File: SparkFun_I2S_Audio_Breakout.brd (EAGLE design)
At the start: 20.3 x 20.3 mm, 42 parts, among them IC1 MAX98375A

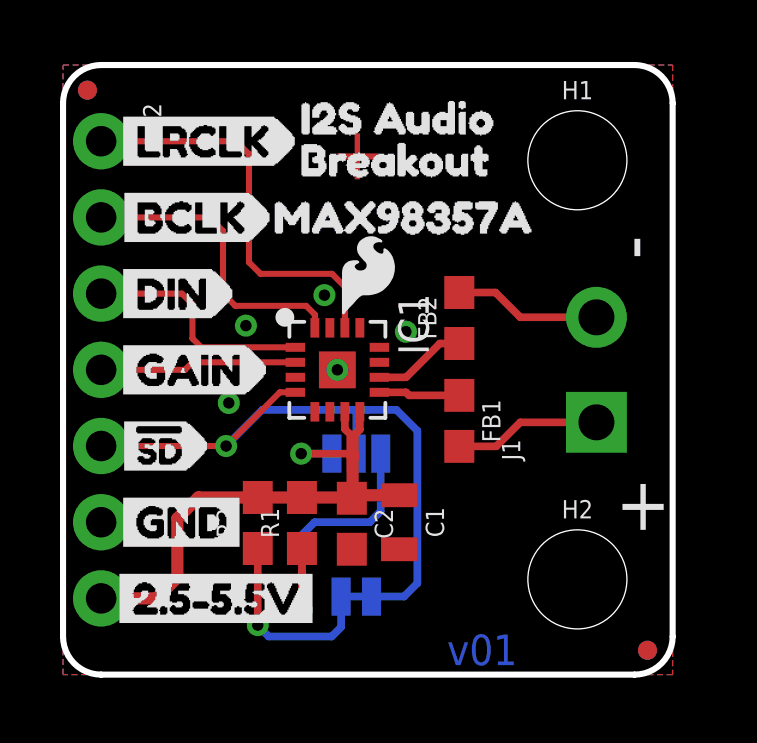
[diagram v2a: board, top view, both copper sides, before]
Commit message: v10
Removed + symbol on top copper
Removed ferrite beads
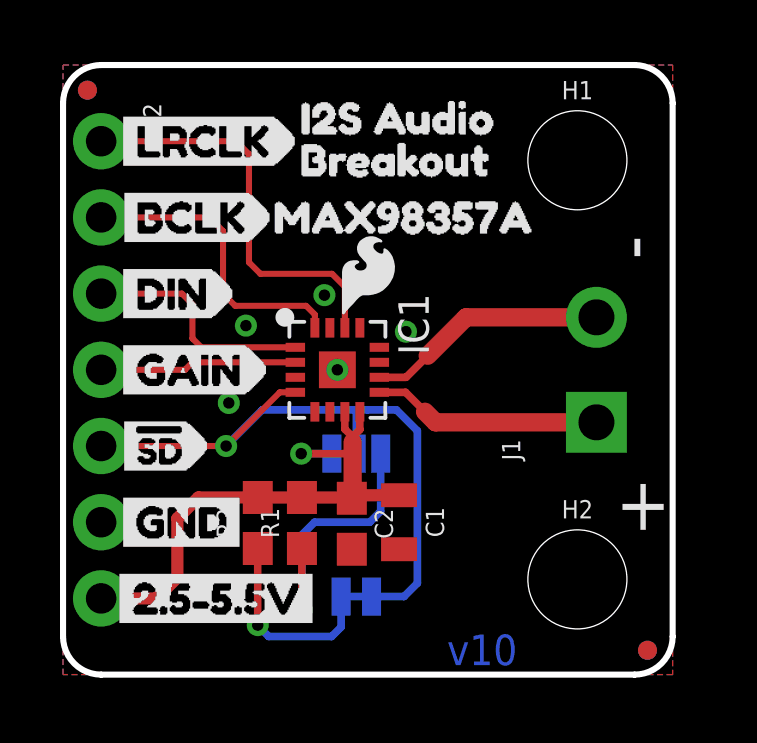
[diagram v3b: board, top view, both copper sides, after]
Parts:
- removed FB1, FB2: (no value), SparkFun-Coils:0603
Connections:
- removed net N$1: FB1.1, IC1.P$9
- removed net N$2: FB2.1, IC1.P$10
- removed net N$3: FB1.2, J1.1
- removed net N$4: FB2.2, J1.2
- new net OUT+: IC1.P$9, J1.1
- new net OUT-: IC1.P$10, J1.2
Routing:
- net OUT-: track 0.00 -> 8.06 mm
- net OUT+: track 0.00 -> 7.65 mm
- net N$4: track 4.92 -> 0.00 mm
- net N$3: track 4.90 -> 0.00 mm
- net N$2: track 3.13 -> 0.00 mm
- net N$1: track 2.85 -> 0.00 mm
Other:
- board text added: "v10"
- board text removed: "v01"
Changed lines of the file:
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@@
 <?xml version="1.0" encoding="utf-8"?>
 <!DOCTYPE eagle SYSTEM "eagle.dtd">
-<eagle version="9.0.1">
+<eagle version="9.1.1">
 <drawing>
 <settings>
@@
 <wire x1="9.865359375" y1="10.287" x2="9.865359375" y2="10.033" width="0.2032" layer="41"/>
 <wire x1="9.017" y1="9.44118125" x2="9.271" y2="9.44118125" width="0.2032" layer="41"/>
-<text x="13.97" y="0.3175" size="1.016" layer="16" font="vector" ratio="20" rot="SR0" align="bottom-center">v01</text>
+<text x="13.97" y="0.3175" size="1.016" layer="16" font="vector" ratio="20" rot="SR0" align="bottom-center">v10</text>
 <text x="12.7635" y="-18.288" size="2.1844" layer="51" font="vector" ratio="15" align="center-left">Alex Wende</text>
 <dimension x1="0" y1="1.27" x2="20.32" y2="1.27" x3="10.16" y3="-5.08" textsize="1.27" textratio="15" layer="47" unit="inch"/>
@@
 <text x="5.08" y="-6.35" size="1.27" layer="47" font="vector" ratio="15" align="center-left">Units: Inches</text>
 <dimension x1="1.27" y1="2.54" x2="1.27" y2="0" x3="-2.54" y3="1.27" textsize="1.27" textratio="15" layer="47" unit="inch" precision="3"/>
-<text x="8.89" y="16.51" size="1.778" layer="1" font="vector" ratio="16">+</text>
 <text x="18.415" y="4.826" size="1.778" layer="21" font="vector" ratio="15">+</text>
 <text x="19.812" y="13.843" size="1.778" layer="21" font="vector" ratio="15" rot="R90">-</text>
@@
 <param name="checkStop" value="0"/>
 <param name="checkValues" value="0"/>
+<param name="checkNames" value="1"/>
+<param name="checkWireStubs" value="1"/>
+<param name="checkPolygonWidth" value="0"/>
 <param name="useDiameter" value="13"/>
 <param name="maxErrors" value="50"/>
@@
 <attribute name="PROD_ID" value="CAP-00810" x="9.6266" y="5.0292" size="1.778" layer="27" rot="R270" display="off"/>
 </element>
-<element name="FB1" library="SparkFun-Coils" package="0603" value="" x="13.208" y="8.4582" rot="R270">
-<attribute name="PROD_ID" value="NDUC-13805" x="13.208" y="8.4582" size="1.778" layer="27" rot="R270" display="off"/>
-</element>
-<element name="FB2" library="SparkFun-Coils" package="0603" value="" x="13.208" y="11.8872" rot="R90">
-<attribute name="PROD_ID" value="NDUC-13805" x="13.208" y="11.8872" size="1.778" layer="27" rot="R90" display="off"/>
-</element>
 <element name="IC1" library="SparkFun-IC-Amplifiers" package="TQFN-16" value="MAX98375A" x="9.144" y="10.16" rot="R270">
 <attribute name="PROD_ID" value="IC-14032" x="9.144" y="10.16" size="1.778" layer="27" rot="R270" display="off"/>
@@
 </elements>
 <signals>
-<signal name="N$1">
+<signal name="OUT+">
 <contactref element="IC1" pad="P$9"/>
-<contactref element="FB1" pad="1"/>
-<wire x1="10.544" y1="9.41" x2="11.43" y2="9.41" width="0.254" layer="1"/>
-<wire x1="13.1062" y1="9.41" x2="13.208" y2="9.3082" width="0.6096" layer="1"/>
-<wire x1="13.208" y1="9.3082" x2="11.5318" y2="9.3082" width="0.254" layer="1"/>
-<wire x1="11.5318" y1="9.3082" x2="11.43" y2="9.41" width="0.254" layer="1"/>
-</signal>
-<signal name="N$2">
+<contactref element="J1" pad="1"/>
+<wire x1="17.78" y1="8.409940625" x2="12.418059375" y2="8.409940625" width="0.6096" layer="1"/>
+<wire x1="12.418059375" y1="8.409940625" x2="12.065" y2="8.763" width="0.6096" layer="1"/>
+<wire x1="12.065" y1="8.763" x2="11.418" y2="9.41" width="0.254" layer="1"/>
+<wire x1="11.418" y1="9.41" x2="10.544" y2="9.41" width="0.254" layer="1"/>
+</signal>
+<signal name="OUT-">
 <contactref element="IC1" pad="P$10"/>
-<contactref element="FB2" pad="1"/>
-<wire x1="10.544" y1="9.91" x2="11.434" y2="9.91" width="0.254" layer="1"/>
-<wire x1="11.434" y1="9.91" x2="12.5612" y2="11.0372" width="0.254" layer="1"/>
-<wire x1="12.5612" y1="11.0372" x2="13.208" y2="11.0372" width="0.254" layer="1"/>
-</signal>
-<signal name="N$3">
-<contactref element="FB1" pad="2"/>
-<contactref element="J1" pad="1"/>
-<wire x1="13.208" y1="7.6082" x2="14.438259375" y2="7.6082" width="0.254" layer="1"/>
-<wire x1="14.438259375" y1="7.6082" x2="15.24" y2="8.409940625" width="0.254" layer="1"/>
-<wire x1="15.24" y1="8.409940625" x2="17.78" y2="8.409940625" width="0.254" layer="1"/>
-</signal>
-<signal name="N$4">
-<contactref element="FB2" pad="2"/>
 <contactref element="J1" pad="2"/>
-<wire x1="13.208" y1="12.7372" x2="14.4154" y2="12.7372" width="0.254" layer="1"/>
-<wire x1="14.4154" y1="12.7372" x2="15.24" y2="11.9126" width="0.254" layer="1"/>
-<wire x1="15.24" y1="11.9126" x2="17.78" y2="11.9126" width="0.254" layer="1"/>
-<wire x1="17.78" y1="11.9126" x2="17.78" y2="11.909940625" width="0.254" layer="1"/>
+<wire x1="17.78" y1="11.909940625" x2="13.433940625" y2="11.909940625" width="0.6096" layer="1"/>
+<wire x1="13.433940625" y1="11.909940625" x2="12.1539" y2="10.6299" width="0.6096" layer="1"/>
+<wire x1="12.1539" y1="10.6299" x2="11.434" y2="9.91" width="0.254" layer="1"/>
+<wire x1="11.434" y1="9.91" x2="10.544" y2="9.91" width="0.254" layer="1"/>
 </signal>
 <signal name="!SD">
@@
 <wire x1="9.652" y1="7.9248" x2="9.394" y2="8.1828" width="0.254" layer="1"/>
 <wire x1="9.394" y1="8.1828" x2="9.394" y2="8.76" width="0.254" layer="1"/>
-<wire x1="9.652" y1="7.1882" x2="9.652" y2="7.239" width="0.254" layer="1"/>
-<wire x1="9.652" y1="7.366" x2="9.652" y2="7.9248" width="0.254" layer="1"/>
+<wire x1="9.652" y1="7.366" x2="9.652" y2="7.747" width="0.254" layer="1"/>
+<wire x1="9.652" y1="7.747" x2="9.652" y2="7.9248" width="0.254" layer="1"/>
 <wire x1="9.652" y1="7.9375" x2="9.652" y2="7.9248" width="0.254" layer="1"/>
-<wire x1="11.2014" y1="5.98" x2="9.652" y2="5.98" width="0.4064" layer="1"/>
+<wire x1="11.2014" y1="5.98" x2="9.6266" y2="5.98" width="0.4064" layer="1"/>
 <wire x1="9.6266" y1="5.98" x2="9.6266" y2="5.8792" width="0.4064" layer="1"/>
 <wire x1="9.6266" y1="5.8792" x2="9.6266" y2="5.9046" width="0.4064" layer="1"/>
 <wire x1="9.6266" y1="5.9046" x2="7.9629" y2="5.9046" width="0.4064" layer="1"/>
 <wire x1="7.9629" y1="5.9046" x2="6.4897" y2="5.9046" width="0.4064" layer="1"/>
-<wire x1="9.652" y1="7.9375" x2="9.652" y2="7.366" width="0.4064" layer="1"/>
-<wire x1="9.652" y1="7.366" x2="9.652" y2="7.239" width="0.4064" layer="1"/>
-<wire x1="9.652" y1="7.239" x2="9.652" y2="5.98" width="0.4064" layer="1"/>
-<wire x1="9.652" y1="5.98" x2="9.6266" y2="5.98" width="0.4064" layer="1"/>
 <wire x1="1.27" y1="2.54" x2="3.1115" y2="2.54" width="0.4064" layer="1"/>
 <wire x1="3.1115" y1="2.54" x2="3.81" y2="3.2385" width="0.4064" layer="1"/>
@@
 <via x="7.9375" y="7.366" extent="1-16" drill="0.381"/>
 <wire x1="7.9375" y1="7.366" x2="9.652" y2="7.366" width="0.254" layer="1"/>
+<wire x1="9.6266" y1="5.8792" x2="9.652" y2="5.9046" width="0.6096" layer="1"/>
+<wire x1="9.652" y1="5.9046" x2="9.652" y2="7.747" width="0.6096" layer="1"/>
 </signal>
 <signal name="GND">
@@
 </signal>
 </signals>
+<mfgpreviewcolors>
+<mfgpreviewcolor name="soldermaskcolor" color="0xC8008000"/>
+<mfgpreviewcolor name="silkscreencolor" color="0xFFFEFEFE"/>
+<mfgpreviewcolor name="backgroundcolor" color="0xFF282828"/>
+<mfgpreviewcolor name="coppercolor" color="0xFFFFBF00"/>
+<mfgpreviewcolor name="substratecolor" color="0xFF786E46"/>
+</mfgpreviewcolors>
 <errors>
 </errors>

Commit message: v10 panel
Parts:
- removed FRAME1: FRAME-LETTER, SparkFun-Aesthetics:CREATIVE_COMMONS
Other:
- board text removed: "Alex Wende"
- board text removed: "Units: Inches"
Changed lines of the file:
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@@
 <?xml version="1.0" encoding="utf-8"?>
 <!DOCTYPE eagle SYSTEM "eagle.dtd">
-<eagle version="9.1.1">
+<eagle version="9.1.0">
 <drawing>
 <settings>
@@
 <setting verticaltext="up"/>
 </settings>
-<grid distance="50" unitdist="mil" unit="inch" style="lines" multiple="1" display="yes" altdistance="0.005" altunitdist="inch" altunit="inch"/>
+<grid distance="0.05" unitdist="inch" unit="inch" style="lines" multiple="1" display="yes" altdistance="0.005" altunitdist="inch" altunit="inch"/>
 <layers>
 <layer number="1" name="Top" color="4" fill="1" visible="yes" active="yes"/>
@@
 <layer number="23" name="tOrigins" color="15" fill="1" visible="yes" active="yes"/>
 <layer number="24" name="bOrigins" color="15" fill="1" visible="yes" active="yes"/>
-<layer number="25" name="tNames" color="7" fill="1" visible="no" active="yes"/>
-<layer number="26" name="bNames" color="7" fill="1" visible="no" active="yes"/>
-<layer number="27" name="tValues" color="7" fill="1" visible="no" active="yes"/>
-<layer number="28" name="bValues" color="7" fill="1" visible="no" active="yes"/>
+<layer number="25" name="tNames" color="7" fill="1" visible="yes" active="yes"/>
+<layer number="26" name="bNames" color="7" fill="1" visible="yes" active="yes"/>
+<layer number="27" name="tValues" color="7" fill="1" visible="yes" active="yes"/>
+<layer number="28" name="bValues" color="7" fill="1" visible="yes" active="yes"/>
 <layer number="29" name="tStop" color="7" fill="3" visible="yes" active="yes"/>
-<layer number="30" name="bStop" color="7" fill="6" visible="no" active="yes"/>
-<layer number="31" name="tCream" color="7" fill="4" visible="no" active="yes"/>
-<layer number="32" name="bCream" color="7" fill="5" visible="no" active="yes"/>
-<layer number="33" name="tFinish" color="6" fill="3" visible="no" active="yes"/>
-<layer number="34" name="bFinish" color="6" fill="6" visible="no" active="yes"/>
-<layer number="35" name="tGlue" color="7" fill="4" visible="no" active="yes"/>
-<layer number="36" name="bGlue" color="7" fill="5" visible="no" active="yes"/>
-<layer number="37" name="tTest" color="7" fill="1" visible="no" active="yes"/>
-<layer number="38" name="bTest" color="7" fill="1" visible="no" active="yes"/>
+<layer number="30" name="bStop" color="7" fill="6" visible="yes" active="yes"/>
+<layer number="31" name="tCream" color="7" fill="4" visible="yes" active="yes"/>
+<layer number="32" name="bCream" color="7" fill="5" visible="yes" active="yes"/>
+<layer number="33" name="tFinish" color="6" fill="3" visible="yes" active="yes"/>
+<layer number="34" name="bFinish" color="6" fill="6" visible="yes" active="yes"/>
+<layer number="35" name="tGlue" color="7" fill="4" visible="yes" active="yes"/>
+<layer number="36" name="bGlue" color="7" fill="5" visible="yes" active="yes"/>
+<layer number="37" name="tTest" color="7" fill="1" visible="yes" active="yes"/>
+<layer number="38" name="bTest" color="7" fill="1" visible="yes" active="yes"/>
 <layer number="39" name="tKeepout" color="4" fill="11" visible="yes" active="yes"/>
 <layer number="40" name="bKeepout" color="1" fill="11" visible="yes" active="yes"/>
@@
 <layer number="42" name="bRestrict" color="1" fill="10" visible="yes" active="yes"/>
 <layer number="43" name="vRestrict" color="2" fill="10" visible="yes" active="yes"/>
-<layer number="44" name="Drills" color="7" fill="1" visible="no" active="yes"/>
-<layer number="45" name="Holes" color="7" fill="1" visible="no" active="yes"/>
-<layer number="46" name="Milling" color="3" fill="1" visible="no" active="yes"/>
-<layer number="47" name="Measures" color="7" fill="1" visible="no" active="yes"/>
+<layer number="44" name="Drills" color="7" fill="1" visible="yes" active="yes"/>
+<layer number="45" name="Holes" color="7" fill="1" visible="yes" active="yes"/>
+<layer number="46" name="Milling" color="3" fill="1" visible="yes" active="yes"/>
+<layer number="47" name="Measures" color="7" fill="1" visible="yes" active="yes"/>
 <layer number="48" name="Document" color="7" fill="1" visible="yes" active="yes"/>
 <layer number="49" name="Reference" color="7" fill="1" visible="yes" active="yes"/>
@@
 <wire x1="9.017" y1="9.44118125" x2="9.271" y2="9.44118125" width="0.2032" layer="41"/>
 <text x="13.97" y="0.3175" size="1.016" layer="16" font="vector" ratio="20" rot="SR0" align="bottom-center">v10</text>
-<text x="12.7635" y="-18.288" size="2.1844" layer="51" font="vector" ratio="15" align="center-left">Alex Wende</text>
-<dimension x1="0" y1="1.27" x2="20.32" y2="1.27" x3="10.16" y3="-5.08" textsize="1.27" textratio="15" layer="47" unit="inch"/>
-<dimension x1="1.27" y1="0" x2="1.27" y2="20.32" x3="-5.08" y3="10.16" textsize="1.27" textratio="15" layer="47" unit="inch"/>
-<dimension x1="0" y1="1.27" x2="1.27" y2="1.27" x3="0.635" y3="-2.54" textsize="1.27" textratio="15" layer="47" unit="inch"/>
-<dimension x1="17.145" y1="3.175" x2="20.32" y2="3.175" x3="18.7325" y3="-2.54" textsize="1.27" textratio="15" layer="47" unit="inch" precision="3"/>
-<dimension x1="17.145" y1="17.145" x2="20.32" y2="17.145" x3="18.7325" y3="22.86" textsize="1.27" textratio="15" layer="47" unit="inch" precision="3"/>
-<dimension x1="17.145" y1="17.145" x2="17.145" y2="20.32" x3="29.21" y3="18.7325" textsize="1.27" textratio="15" layer="47" unit="inch" precision="3"/>
-<dimension x1="17.145" y1="3.175" x2="17.145" y2="0" x3="29.21" y3="1.5875" textsize="1.27" textratio="15" layer="47" unit="inch" precision="3"/>
-<dimension x1="1.27" y1="19.05" x2="0.338125" y2="19.912846875" x3="-5.3852125" y3="25.212228125" textsize="1.27" textratio="15" layer="47" dtype="radius" unit="inch" precision="3"/>
-<text x="5.08" y="-6.35" size="1.27" layer="47" font="vector" ratio="15" align="center-left">Units: Inches</text>
-<dimension x1="1.27" y1="2.54" x2="1.27" y2="0" x3="-2.54" y3="1.27" textsize="1.27" textratio="15" layer="47" unit="inch" precision="3"/>
 <text x="18.415" y="4.826" size="1.778" layer="21" font="vector" ratio="15">+</text>
 <text x="19.812" y="13.843" size="1.778" layer="21" font="vector" ratio="15" rot="R90">-</text>
@@
 <element name="FD1" library="SparkFun-Aesthetics" package="FIDUCIAL-MICRO" value="FIDUCIALUFIDUCIAL" x="19.4818" y="0.8128"/>
 <element name="FD2" library="SparkFun-Aesthetics" package="FIDUCIAL-MICRO" value="FIDUCIALUFIDUCIAL" x="0.8128" y="19.4818"/>
-<element name="FRAME1" library="SparkFun-Aesthetics" package="CREATIVE_COMMONS" value="FRAME-LETTER" x="-13.97" y="-19.05"/>
 <element name="LOGO1" library="SparkFun-Aesthetics" package="SFE_LOGO_NAME_FLAME_.1" value="SFE_LOGO_NAME_FLAME.1_INCH" x="16.891" y="16.129" rot="SMR270"/>
 <element name="LOGO2" library="SparkFun-Aesthetics" package="OSHW-LOGO-S" value="OSHW-LOGOS" x="12.573" y="13.462" rot="MR270"/>
